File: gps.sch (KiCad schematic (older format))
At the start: 1 part, among them U10 LINX-FM-GPS

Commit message: More connections
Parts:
- U10: footprint (none) -> buq2:LINX-FM-GPS
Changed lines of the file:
@@
 F 0 "U10" H 5900 4100 60  0000 C CNN
 F 1 "LINX-FM-GPS" H 5900 2500 60  0000 C CNN
-F 2 "" H 5650 3200 60  0000 C CNN
+F 2 "buq2:LINX-FM-GPS" H 5650 3200 60  0001 C CNN
 F 3 "" H 5650 3200 60  0000 C CNN
 	1    5900 3350
@@
 RX
 $Comp
-L GND #PWR30
+L GND #PWR032
 U 1 1 54616ADD
 P 5250 3350
-F 0 "#PWR30" H 5250 3350 30  0001 C CNN
+F 0 "#PWR032" H 5250 3350 30  0001 C CNN
 F 1 "GND" H 5250 3280 30  0001 C CNN
 F 2 "" H 5250 3350 60  0000 C CNN
@@
 $EndComp
 $Comp
-L GND #PWR33
+L GND #PWR033
 U 1 1 54616AF6
 P 6550 3350
-F 0 "#PWR33" H 6550 3350 30  0001 C CNN
+F 0 "#PWR033" H 6550 3350 30  0001 C CNN
 F 1 "GND" H 6550 3280 30  0001 C CNN
 F 2 "" H 6550 3350 60  0000 C CNN
@@
 VOUT not used for \npassive antennas
 $Comp
-L GND #PWR31
+L GND #PWR034
 U 1 1 5461790A
 P 6550 2850
-F 0 "#PWR31" H 6550 2850 30  0001 C CNN
+F 0 "#PWR034" H 6550 2850 30  0001 C CNN
 F 1 "GND" H 6550 2780 30  0001 C CNN
 F 2 "" H 6550 2850 60  0000 C CNN
@@
 $EndComp
 $Comp
-L GND #PWR32
+L GND #PWR035
 U 1 1 5461791F
 P 6550 3050
-F 0 "#PWR32" H 6550 3050 30  0001 C CNN
+F 0 "#PWR035" H 6550 3050 30  0001 C CNN
 F 1 "GND" H 6550 2980 30  0001 C CNN
 F 2 "" H 6550 3050 60  0000 C CNN

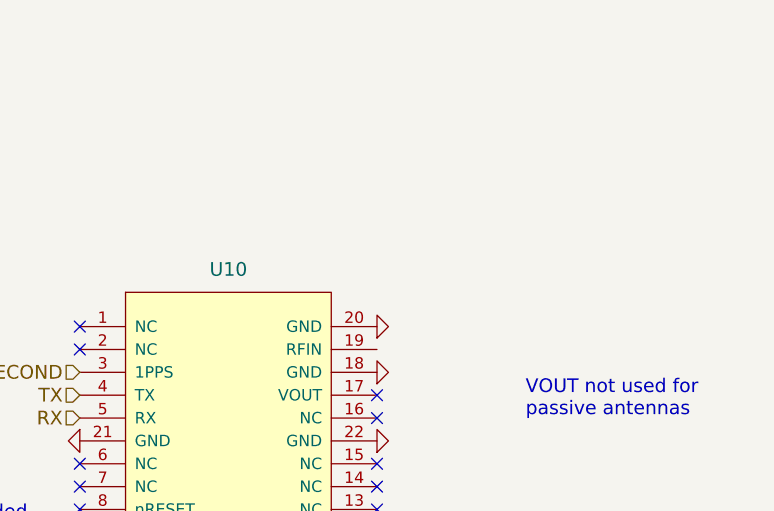
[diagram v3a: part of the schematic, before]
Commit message: Add buttons. Fix DRC. Add antenna
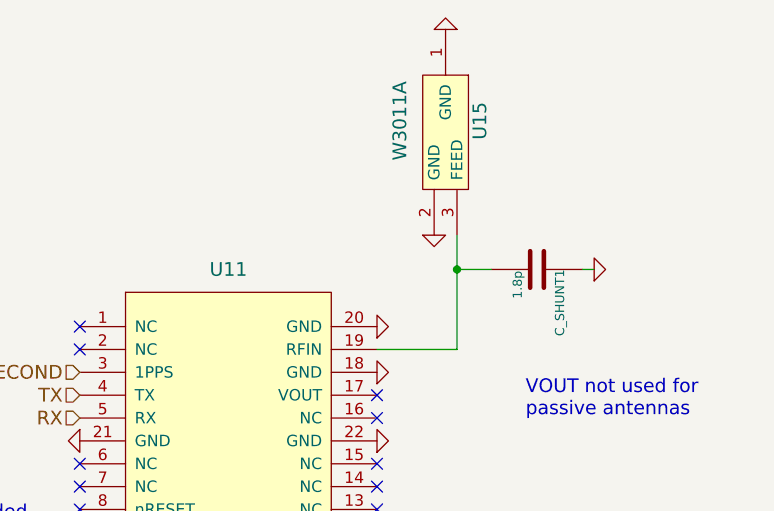
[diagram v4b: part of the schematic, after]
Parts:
- added C_SHUNT1: 1.8p, symbol C
- added U15: W3011A, symbol W3011A
- renumbered U10 to U11
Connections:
- net GND: now also C_SHUNT1.1, U15.1 (GND), U15.2 (GND)
- net at U11.19 (RFIN): now also C_SHUNT1.2, U15.3 (FEED)
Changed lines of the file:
@@
 $Descr A4 11693 8268
 encoding utf-8
-Sheet 11 13
+Sheet 11 14
 Title ""
 Date ""
@@
 $EndDescr
 $Comp
-L LINX-FM-GPS U10
+L LINX-FM-GPS U11
 U 1 1 54616A4F
 P 5900 3350
-F 0 "U10" H 5900 4100 60  0000 C CNN
+F 0 "U11" H 5900 4100 60  0000 C CNN
 F 1 "LINX-FM-GPS" H 5900 2500 60  0000 C CNN
 F 2 "buq2:LINX-FM-GPS" H 5650 3200 60  0001 C CNN
@@
 RX
 $Comp
-L GND #PWR033
+L GND #PWR036
 U 1 1 54616ADD
 P 5250 3350
-F 0 "#PWR033" H 5250 3350 30  0001 C CNN
+F 0 "#PWR036" H 5250 3350 30  0001 C CNN
 F 1 "GND" H 5250 3280 30  0001 C CNN
 F 2 "" H 5250 3350 60  0000 C CNN
@@
 $EndComp
 $Comp
-L GND #PWR034
+L GND #PWR037
 U 1 1 54616AF6
 P 6550 3350
-F 0 "#PWR034" H 6550 3350 30  0001 C CNN
+F 0 "#PWR037" H 6550 3350 30  0001 C CNN
 F 1 "GND" H 6550 3280 30  0001 C CNN
 F 2 "" H 6550 3350 60  0000 C CNN
@@
 VOUT not used for \npassive antennas
 $Comp
-L GND #PWR035
+L GND #PWR038
 U 1 1 5461790A
 P 6550 2850
-F 0 "#PWR035" H 6550 2850 30  0001 C CNN
+F 0 "#PWR038" H 6550 2850 30  0001 C CNN
 F 1 "GND" H 6550 2780 30  0001 C CNN
 F 2 "" H 6550 2850 60  0000 C CNN
@@
 $EndComp
 $Comp
-L GND #PWR036
+L GND #PWR039
 U 1 1 5461791F
 P 6550 3050
-F 0 "#PWR036" H 6550 3050 30  0001 C CNN
+F 0 "#PWR039" H 6550 3050 30  0001 C CNN
 F 1 "GND" H 6550 2980 30  0001 C CNN
 F 2 "" H 6550 3050 60  0000 C CNN
@@
 	0    -1   -1   0
 $EndComp
+$Comp
+L GND #PWR040
+U 1 1 5463B9B3
+P 6850 1550
+F 0 "#PWR040" H 6850 1550 30  0001 C CNN
+F 1 "GND" H 6850 1480 30  0001 C CNN
+F 2 "" H 6850 1550 60  0000 C CNN
+F 3 "" H 6850 1550 60  0000 C CNN
+	1    6850 1550
+	-1   0    0    1
+$EndComp
+$Comp
+L GND #PWR041
+U 1 1 5463B9C7
+P 6800 2450
+F 0 "#PWR041" H 6800 2450 30  0001 C CNN
+F 1 "GND" H 6800 2380 30  0001 C CNN
+F 2 "" H 6800 2450 60  0000 C CNN
+F 3 "" H 6800 2450 60  0000 C CNN
+	1    6800 2450
+	1    0    0    -1
+$EndComp
+Wire Wire Line
+	6550 2950 6900 2950
+Wire Wire Line
+	6900 2950 6900 2450
+$Comp
+L W3011A U15
+U 1 1 5463BF79
+P 6850 1950
+F 0 "U15" H 6850 2100 60  0000 C CNN
+F 1 "W3011A" H 6850 1750 60  0000 C CNN
+F 2 "" H 6850 1950 60  0000 C CNN
+F 3 "" H 6850 1950 60  0000 C CNN
+	1    6850 1950
+	0    1    1    0
+$EndComp
+$Comp
+L C C_SHUNT1
+U 1 1 5463C025
+P 7250 2600
+F 0 "C_SHUNT1" H 7250 2700 40  0000 L CNN
+F 1 "1.8p" H 7256 2515 40  0000 L CNN
+F 2 "" H 7288 2450 30  0000 C CNN
+F 3 "" H 7250 2600 60  0000 C CNN
+	1    7250 2600
+	0    1    1    0
+$EndComp
+$Comp
+L GND #PWR042
+U 1 1 5463C26A
+P 7500 2600
+F 0 "#PWR042" H 7500 2600 30  0001 C CNN
+F 1 "GND" H 7500 2530 30  0001 C CNN
+F 2 "" H 7500 2600 60  0000 C CNN
+F 3 "" H 7500 2600 60  0000 C CNN
+	1    7500 2600
+	0    -1   -1   0
+$EndComp
+Wire Wire Line
+	7050 2600 6900 2600
+Connection ~ 6900 2600
+Wire Wire Line
+	7450 2600 7500 2600
 $EndSCHEMATC

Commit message: Start first layout test
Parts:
- C_SHUNT1: footprint (none) -> buq2:SM0603
- U15: footprint (none) -> buq2:W3011A
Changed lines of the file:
@@
 F 0 "U15" H 6850 2100 60  0000 C CNN
 F 1 "W3011A" H 6850 1750 60  0000 C CNN
-F 2 "" H 6850 1950 60  0000 C CNN
+F 2 "buq2:W3011A" H 6850 1950 60  0001 C CNN
 F 3 "" H 6850 1950 60  0000 C CNN
 	1    6850 1950
@@
 F 0 "C_SHUNT1" H 7250 2700 40  0000 L CNN
 F 1 "1.8p" H 7256 2515 40  0000 L CNN
-F 2 "" H 7288 2450 30  0000 C CNN
+F 2 "buq2:SM0603" H 7288 2450 30  0001 C CNN
 F 3 "" H 7250 2600 60  0000 C CNN
 	1    7250 2600

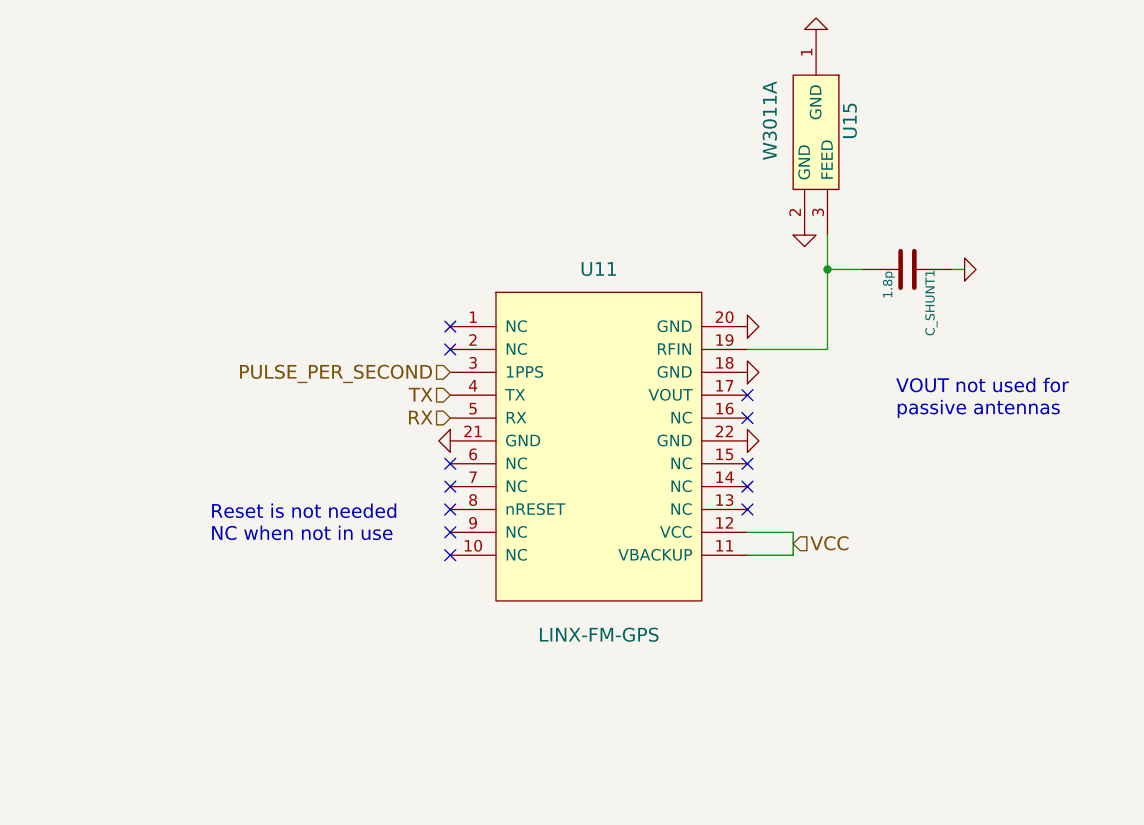
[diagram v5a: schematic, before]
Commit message: Before making larger board. - Changed GPS module
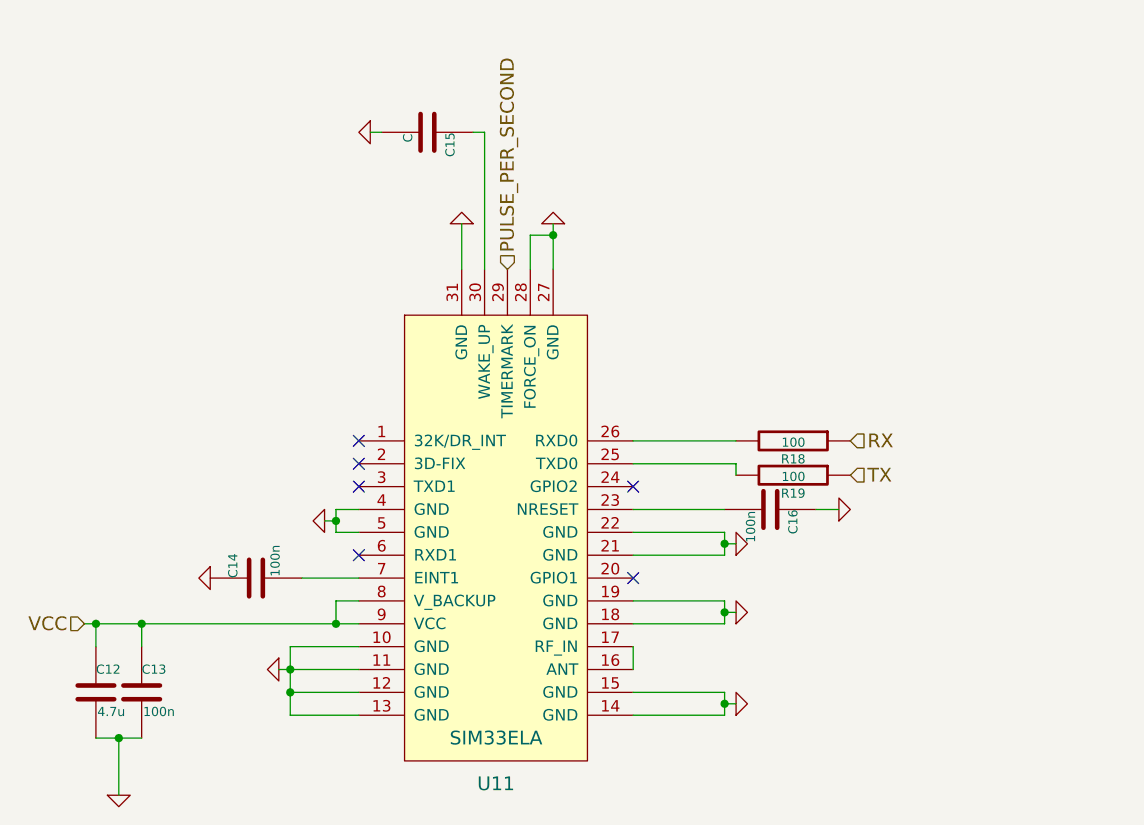
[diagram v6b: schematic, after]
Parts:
- removed C_SHUNT1: 1.8p, buq2:SM0603, symbol C
- removed U11: LINX-FM-GPS, buq2:LINX-FM-GPS, symbol LINX-FM-GPS
- removed U15: W3011A, buq2:W3011A, symbol W3011A
- added C12: 4.7u, symbol C
- added C13, C14, C16: 100n, symbol C
- added C15: C, symbol C
- added R18, R19: 100, symbol R
- added U11: SIM33ELA, symbol SIM33ELA
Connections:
- net GND: now also C12.2, C13.2, C14.1, C15.2, C16.1, U11.10 (GND), U11.11 (GND), U11.12 (GND), U11.13 (GND), U11.14 (GND), U11.15 (GND), U11.18 (GND), U11.19 (GND), U11.21 (GND), U11.22 (GND), U11.27 (GND), U11.28 (FORCE_ON), U11.31 (GND), U11.4 (GND), U11.5 (GND)
- net PULSE_PER_SECOND: now also U11.29 (TIMERMARK)
- net RX: now also R18.1
- net TX: now also R19.1
- net VCC: now also C12.1, C13.1, U11.8 (V_BACKUP), U11.9 (VCC)
- new net: U11.16 (ANT), U11.17 (RF_IN)
- new net: C16.2, U11.23 (NRESET)
- new net: R19.2, U11.25 (TXD0)
- new net: R18.2, U11.26 (RXD0)
- new net: C15.1, U11.30 (WAKE_UP)
- new net: C14.2, U11.7 (EINT1)
- no-connect marks 12 -> 6
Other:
- note removed: "Reset is not needed\nNC when not in use"
- note removed: "VOUT not used for \npassive antennas"

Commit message: Before adding proper reset and battery monitor
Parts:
- C12: footprint (none) -> buq2:SM0805
- C13, C14, C16, R18, R19: footprint (none) -> buq2:SM0603
- C15: value C -> 100n; footprint (none) -> buq2:SM0603
- U11: footprint (none) -> buq2:SIM33ELA-GPS
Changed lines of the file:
@@
 F 0 "U11" H 5450 2750 60  0000 C CNN
 F 1 "SIM33ELA" H 5450 2950 60  0000 C CNN
-F 2 "" H 5550 3800 60  0000 C CNN
+F 2 "buq2:SIM33ELA-GPS" H 5550 3800 60  0001 C CNN
 F 3 "" H 5550 3800 60  0000 C CNN
 	1    5550 3800
@@
 F 0 "C14" H 4400 4050 40  0000 L CNN
 F 1 "100n" H 4406 3865 40  0000 L CNN
-F 2 "" H 4438 3800 30  0000 C CNN
+F 2 "buq2:SM0603" H 4438 3800 30  0001 C CNN
 F 3 "" H 4400 3950 60  0000 C CNN
 	1    4400 3950
@@
 F 0 "C12" H 3700 4550 40  0000 L CNN
 F 1 "4.7u" H 3706 4365 40  0000 L CNN
-F 2 "" H 3738 4300 30  0000 C CNN
+F 2 "buq2:SM0805" H 3738 4300 30  0001 C CNN
 F 3 "" H 3700 4450 60  0000 C CNN
 	1    3700 4450
@@
 F 0 "C13" H 3900 4550 40  0000 L CNN
 F 1 "100n" H 3906 4365 40  0000 L CNN
-F 2 "" H 3938 4300 30  0000 C CNN
+F 2 "buq2:SM0603" H 3938 4300 30  0001 C CNN
 F 3 "" H 3900 4450 60  0000 C CNN
 	1    3900 4450
@@
 F 0 "C16" H 6650 3750 40  0000 L CNN
 F 1 "100n" H 6656 3565 40  0000 L CNN
-F 2 "" H 6688 3500 30  0000 C CNN
+F 2 "buq2:SM0603" H 6688 3500 30  0001 C CNN
 F 3 "" H 6650 3650 60  0000 C CNN
 	1    6650 3650
@@
 F 0 "R18" V 6830 3350 40  0000 C CNN
 F 1 "100" V 6757 3351 40  0000 C CNN
-F 2 "" V 6680 3350 30  0000 C CNN
+F 2 "buq2:SM0603" V 6680 3350 30  0001 C CNN
 F 3 "" H 6750 3350 30  0000 C CNN
 	1    6750 3350
@@
 F 0 "R19" V 6830 3500 40  0000 C CNN
 F 1 "100" V 6757 3501 40  0000 C CNN
-F 2 "" V 6680 3500 30  0000 C CNN
+F 2 "buq2:SM0603" V 6680 3500 30  0001 C CNN
 F 3 "" H 6750 3500 30  0000 C CNN
 	1    6750 3500
@@
 P 5150 2000
 F 0 "C15" H 5150 2100 40  0000 L CNN
-F 1 "C" H 5156 1915 40  0000 L CNN
-F 2 "" H 5188 1850 30  0000 C CNN
+F 1 "100n" H 5156 1915 40  0000 L CNN
+F 2 "buq2:SM0603" H 5188 1850 30  0001 C CNN
 F 3 "" H 5150 2000 60  0000 C CNN
 	1    5150 2000
